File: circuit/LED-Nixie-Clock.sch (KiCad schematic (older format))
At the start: 35 parts, among them J1 USB Micro, J3 Boot, SW1 Reset, U1 MCP1700-3302E_SOT23, U2 STM32F103C8Tx, Y1 8MHz, Y2 32.768kHz

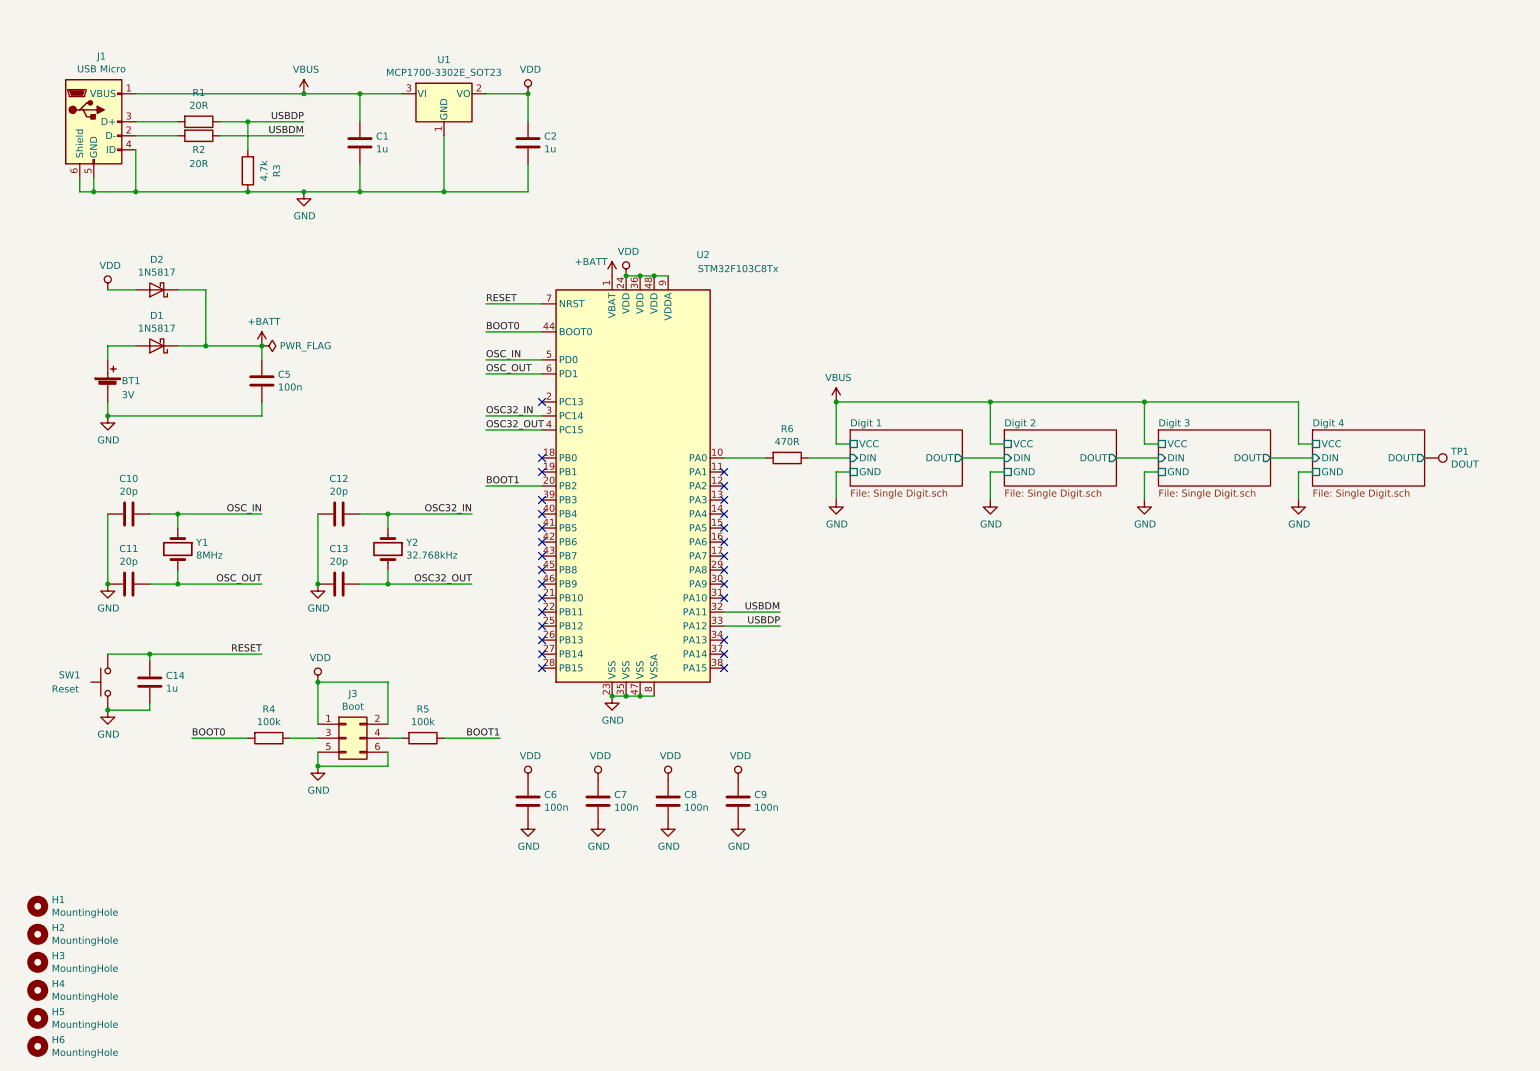
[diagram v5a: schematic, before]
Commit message: Fix oscillator capacitances
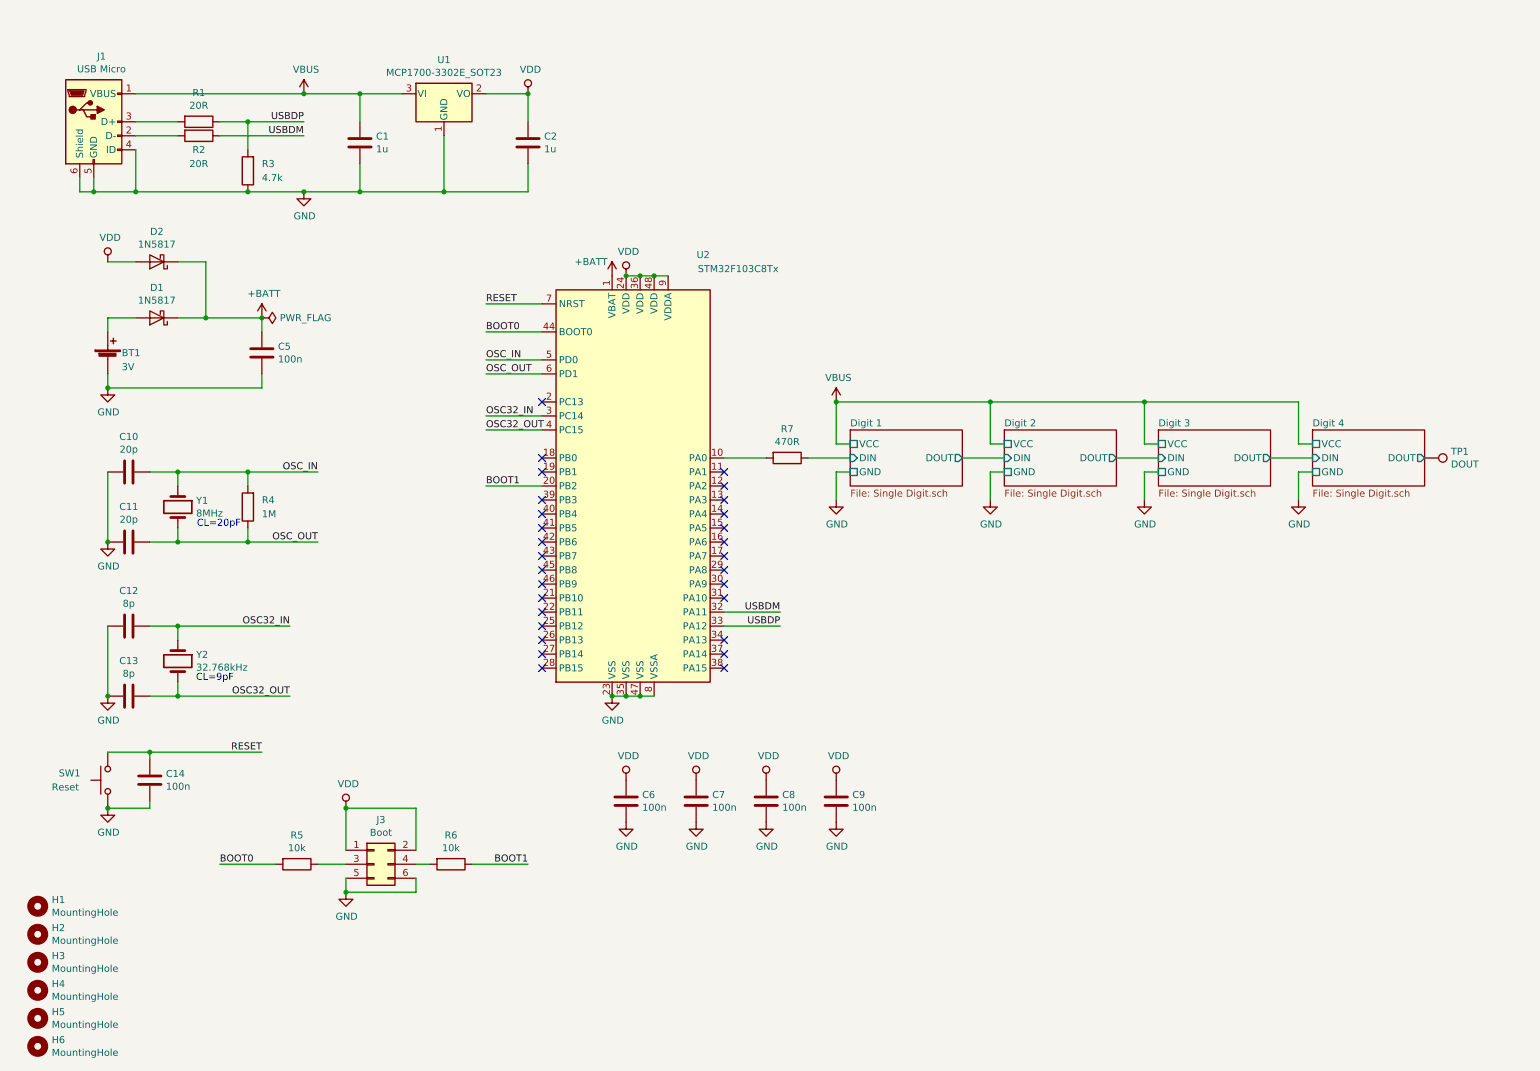
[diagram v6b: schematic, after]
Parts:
- added R4: 1M, Resistor_SMD:R_0805_2012Metric_Pad1.15x1.40mm_HandSolder, symbol Device:R
- C12, C13: value 20p -> 8p
- C14: value 1u -> 100n
- R5: renamed from R4; value 100k -> 10k
- R6: renamed from R5; value 100k -> 10k
- renumbered R6 to R7
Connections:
- net OSC_IN: now also R4.2
- net OSC_OUT: now also R4.1
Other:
- note added: "CL=20pF"
- note added: "CL=9pF"
- moved on the sheet: BT1, C10, C11, C12, C13, C14, C5, C6, C7, C8, C9, D1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

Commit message: Add SWD/JTAG debug port
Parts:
- added J2: Debug, Connector_PinHeader_1.27mm:PinHeader_2x05_P1.27mm_Vertical_SMD, symbol Connector:Conn_ARM_JTAG_SWD_10
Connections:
- net GND: now also J2.3 (GND), J2.5 (GND), J2.9 (GNDDetect)
- net RESET: now also J2.10 (~RESET~)
- net VDD: now also J2.1 (VCC)
- net SWDIO-JTMS: now reaches U2.34 (PA13)
- net SWDIO-JTMS: now also J2.2 (SWDIO/TMS)
- net SWCLK-JTCK: now reaches U2.37 (PA14)
- net SWCLK-JTCK: now also J2.4 (SWDCLK/TCK)
- net JTDI: now reaches U2.38 (PA15)
- net JTDI: now also J2.8 (NC/TDI)
- net SWO-JTDO: now reaches U2.39 (PB3)
- net SWO-JTDO: now also J2.6 (SWO/TDO)
- no-connect marks 29 -> 25
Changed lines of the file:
@@
 NoConn ~ 4200 3500
 NoConn ~ 4200 3600
-NoConn ~ 4200 3800
 NoConn ~ 4200 3900
 NoConn ~ 4200 4000
@@
 NoConn ~ 4200 4900
 NoConn ~ 4200 5000
-NoConn ~ 5500 5000
-NoConn ~ 5500 4900
-NoConn ~ 5500 4800
 NoConn ~ 5500 4500
 NoConn ~ 5500 4400
@@
 Text Notes 2000 5100 2    50   ~ 0
 CL=9pF
+$Comp
+L power:GND #PWR0167
+U 1 1 5CA52352
+P 7400 2200
+F 0 "#PWR0167" H 7400 1950 50  0001 C CNN
+F 1 "GND" H 7405 2027 50  0000 C CNN
+F 2 "" H 7400 2200 50  0001 C CNN
+F 3 "" H 7400 2200 50  0001 C CNN
+	1    7400 2200
+	1    0    0    -1
+$EndComp
+$Comp
+L power:VDD #PWR0169
+U 1 1 5CA5EDA9
+P 7400 1000
+F 0 "#PWR0169" H 7400 850 50  0001 C CNN
+F 1 "VDD" H 7417 1173 50  0000 C CNN
+F 2 "" H 7400 1000 50  0001 C CNN
+F 3 "" H 7400 1000 50  0001 C CNN
+	1    7400 1000
+	1    0    0    -1
+$EndComp
+Text Label 8500 1300 2    50   ~ 0
+RESET
+Text Label 8500 1600 2    50   ~ 0
+SWDIO-JTMS
+Text Label 8500 1500 2    50   ~ 0
+SWCLK-JTCK
+Text Label 8500 1700 2    50   ~ 0
+SWO-JTDO
+$Comp
+L Connector:Conn_ARM_JTAG_SWD_10 J2
+U 1 1 5CA91980
+P 7400 1600
+F 0 "J2" H 6960 1646 50  0000 R CNN
+F 1 "Debug" H 6960 1555 50  0000 R CNN
+F 2 "Connector_PinHeader_1.27mm:PinHeader_2x05_P1.27mm_Vertical_SMD" H 7450 1050 50  0001 L TNN
+F 3 "http://infocenter.arm.com/help/topic/com.arm.doc.faqs/attached/13634/cortex_debug_connectors.pdf" V 7050 350 50  0001 C CNN
+	1    7400 1600
+	1    0    0    -1
+$EndComp
+Wire Wire Line
+	7900 1300 8500 1300
+Wire Wire Line
+	7900 1500 8500 1500
+Wire Wire Line
+	7900 1600 8500 1600
+Wire Wire Line
+	7900 1700 8500 1700
+Wire Wire Line
+	7900 1800 8500 1800
+Wire Wire Line
+	7300 2200 7400 2200
+Connection ~ 7400 2200
+Wire Wire Line
+	5500 4800 6100 4800
+Text Label 6100 4800 2    50   ~ 0
+SWDIO-JTMS
+Text Label 8500 1800 2    50   ~ 0
+JTDI
+Wire Wire Line
+	5500 4900 6100 4900
+Text Label 6100 4900 2    50   ~ 0
+SWCLK-JTCK
+Wire Wire Line
+	5500 5000 5900 5000
+Text Label 5900 5000 2    50   ~ 0
+JTDI
+Wire Wire Line
+	4200 3800 3600 3800
+Text Label 3600 3800 0    50   ~ 0
+SWO-JTDO
 $EndSCHEMATC

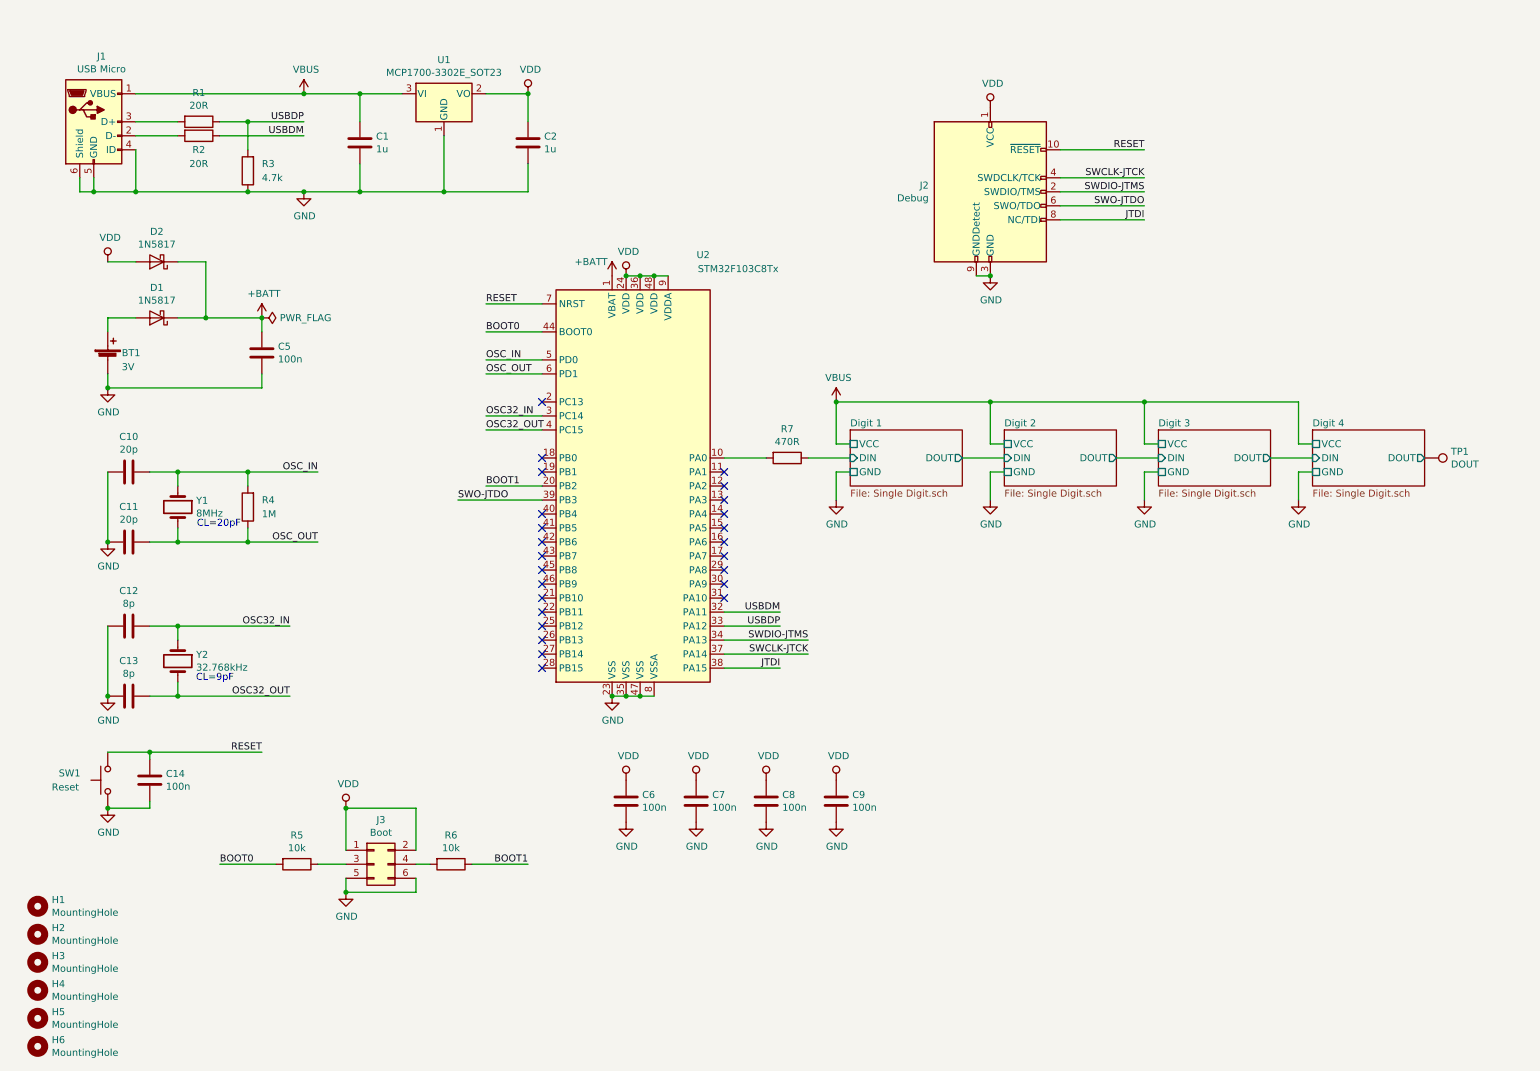
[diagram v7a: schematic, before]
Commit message: Add serial port and replace reset with a boot select pushbutton
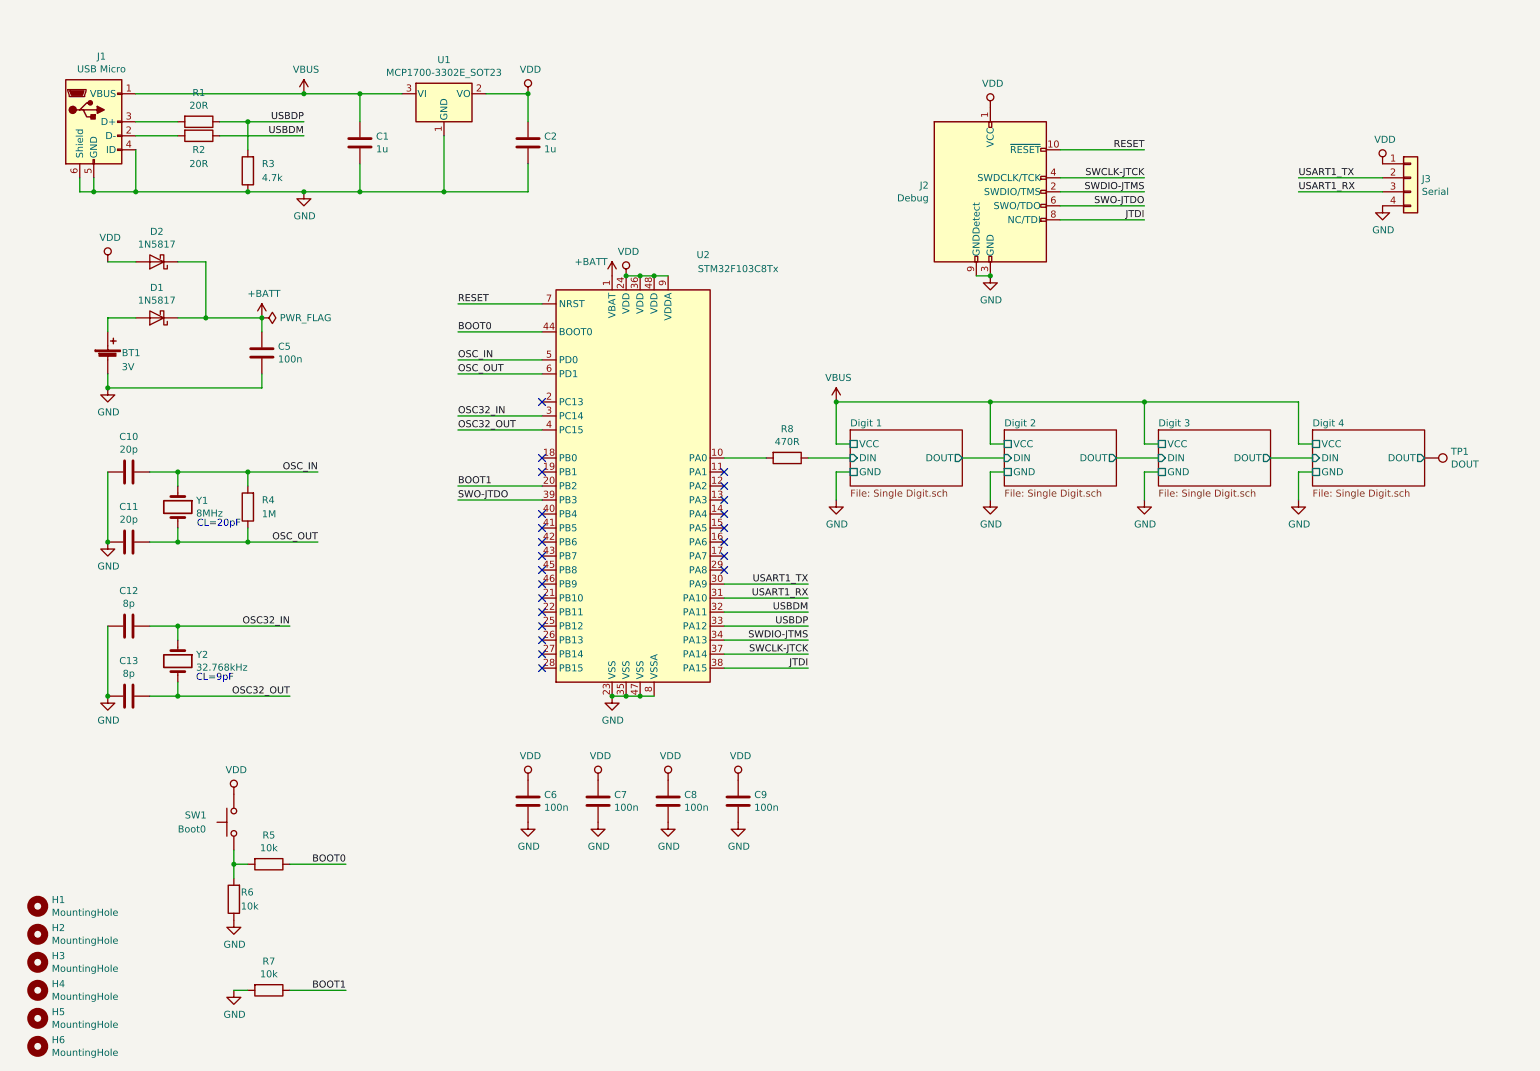
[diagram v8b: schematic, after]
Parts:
- removed C14: 100n, Capacitor_SMD:C_0805_2012Metric_Pad1.15x1.40mm_HandSolder, symbol Device:C
- removed J3: Boot, Connector_PinHeader_2.54mm:PinHeader_2x03_P2.54mm_Vertical, symbol Connector_Generic:Conn_02x03_Odd_Even
- added J3: Serial, Connector_PinHeader_2.54mm:PinHeader_1x04_P2.54mm_Vertical, symbol Connector_Generic:Conn_01x04
- added R7: 10k, Resistor_SMD:R_0805_2012Metric_Pad1.15x1.40mm_HandSolder, symbol Device:R
- SW1: value Reset -> Boot0
- renumbered R7 to R8
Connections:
- net BOOT0: now also R5.1; no longer R5.2
- net BOOT1: now also R7.1; no longer R6.1
- net GND: now also R6.1, J3.4 (Pin_4), R7.2; no longer SW1.1
- net RESET: no longer SW1.2
- net VDD: now also SW1.2, J3.1 (Pin_1)
- net USART1_TX: now reaches U2.30 (PA9)
- net USART1_TX: now also J3.2 (Pin_2)
- net USART1_RX: now reaches U2.31 (PA10)
- net USART1_RX: now also J3.3 (Pin_3)
- net at R6.2: now also R5.2, SW1.1
- no-connect marks 25 -> 23
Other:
- moved on the sheet: C6, C7, C8, C9, SW1
